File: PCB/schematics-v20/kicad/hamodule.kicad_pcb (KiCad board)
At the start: 2 copper layers, 78.4 x 84.3 mm, 104 parts, among them J1 GND|5V, J10 USB_C_Receptacle_USB2.0, J11 2604-1104, J12 2604-1104, J13 EspSense, J2 Conn_01x02_Male, J3 2604-1102, J4 USB | PS, J5 Conn_01x02_Male, J6 GND|3.3V, J7 Conn_01x02_Male, J8 Current Jumper, J9 EspRelays, K1 AQG12205, K2 AQG12205, K3 AQG12205, K4 AQG12205, Q1 SS8050-SMD, Q2 SS8050, SW1 Switch, SW2 Switch, U1 LD1117AV33, U2 ESP32-WROOM-32E, U3 CP2102N-A01-GQFN28, U4 ULN2003A, U5 LDA210-PDIP, U6 LDA210-PDIP, U7 SHT4x

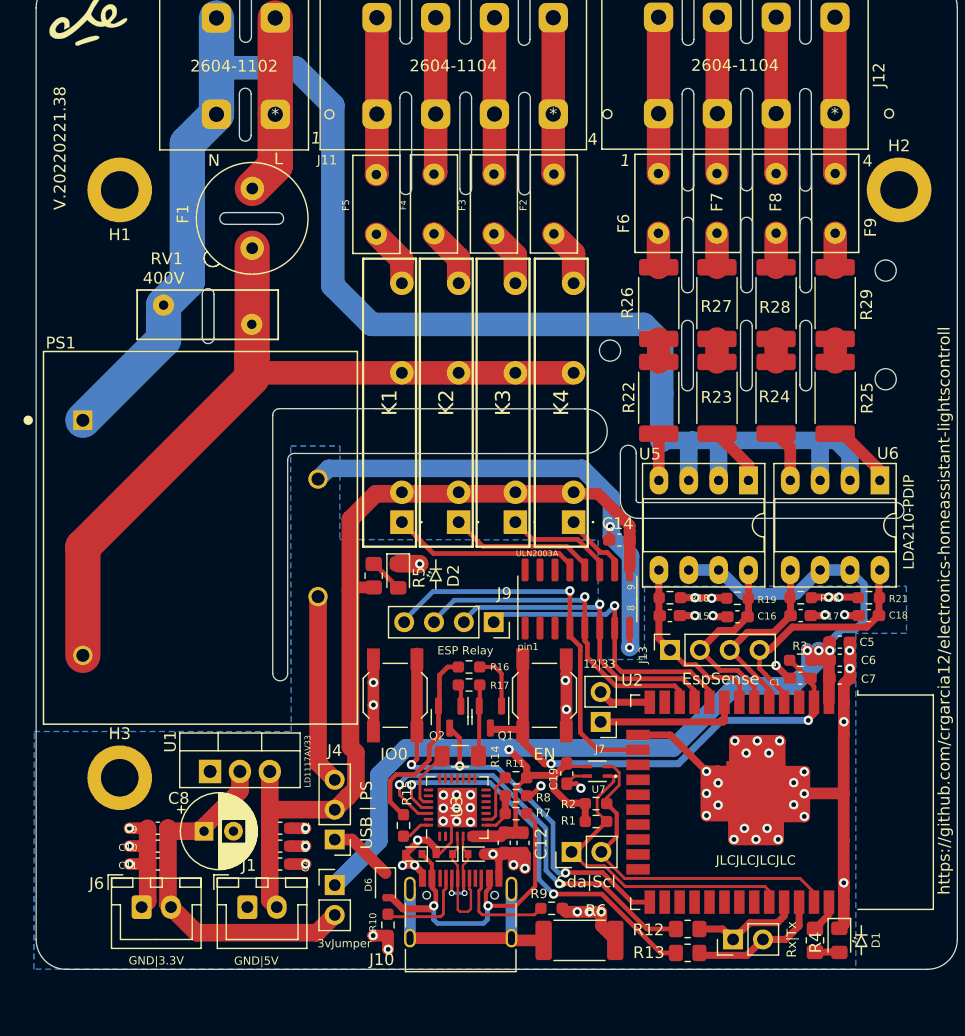
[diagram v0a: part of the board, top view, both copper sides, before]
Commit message: [V20] Move Earth;arrange minors;prod files
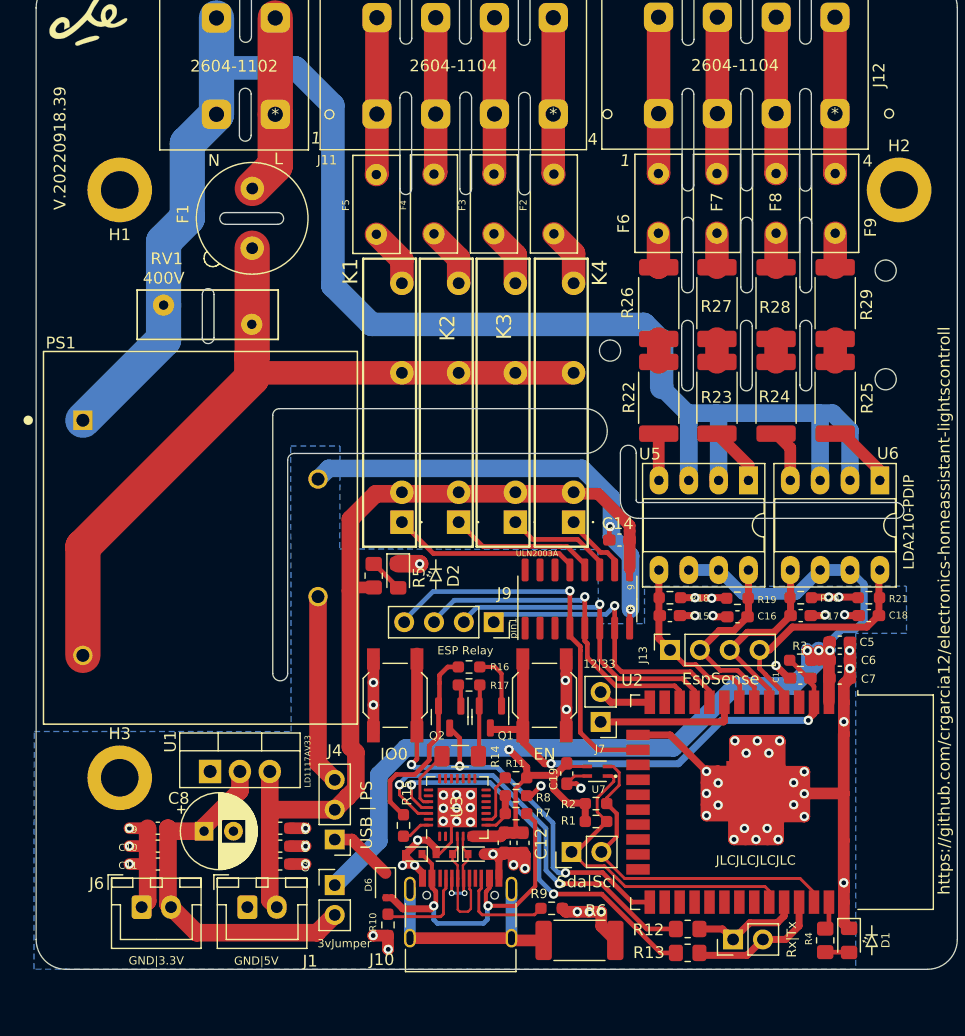
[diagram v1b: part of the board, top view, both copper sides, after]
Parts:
- moved G3 6.21 mm to (136.0, 115.2)
- moved NT1 4.51 mm to (178.4, 100.2)
- moved G2 0.89 mm to (196.1, 149.2)
- moved R4 0.87 mm to (192.3, 149.2)
- moved D1 0.83 mm to (194.3, 149.2)
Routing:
- net 220VAC(N)-LowV: track 29.2 -> 39.1 mm
- net 220VAC(N): track 99.8 -> 95.5 mm
- net GND: track 268.8 -> 265.5 mm
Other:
- outline, holes or cut-outs redrawn
- board text added: "V.20220918.39"
- board text removed: "V.20220221.38"

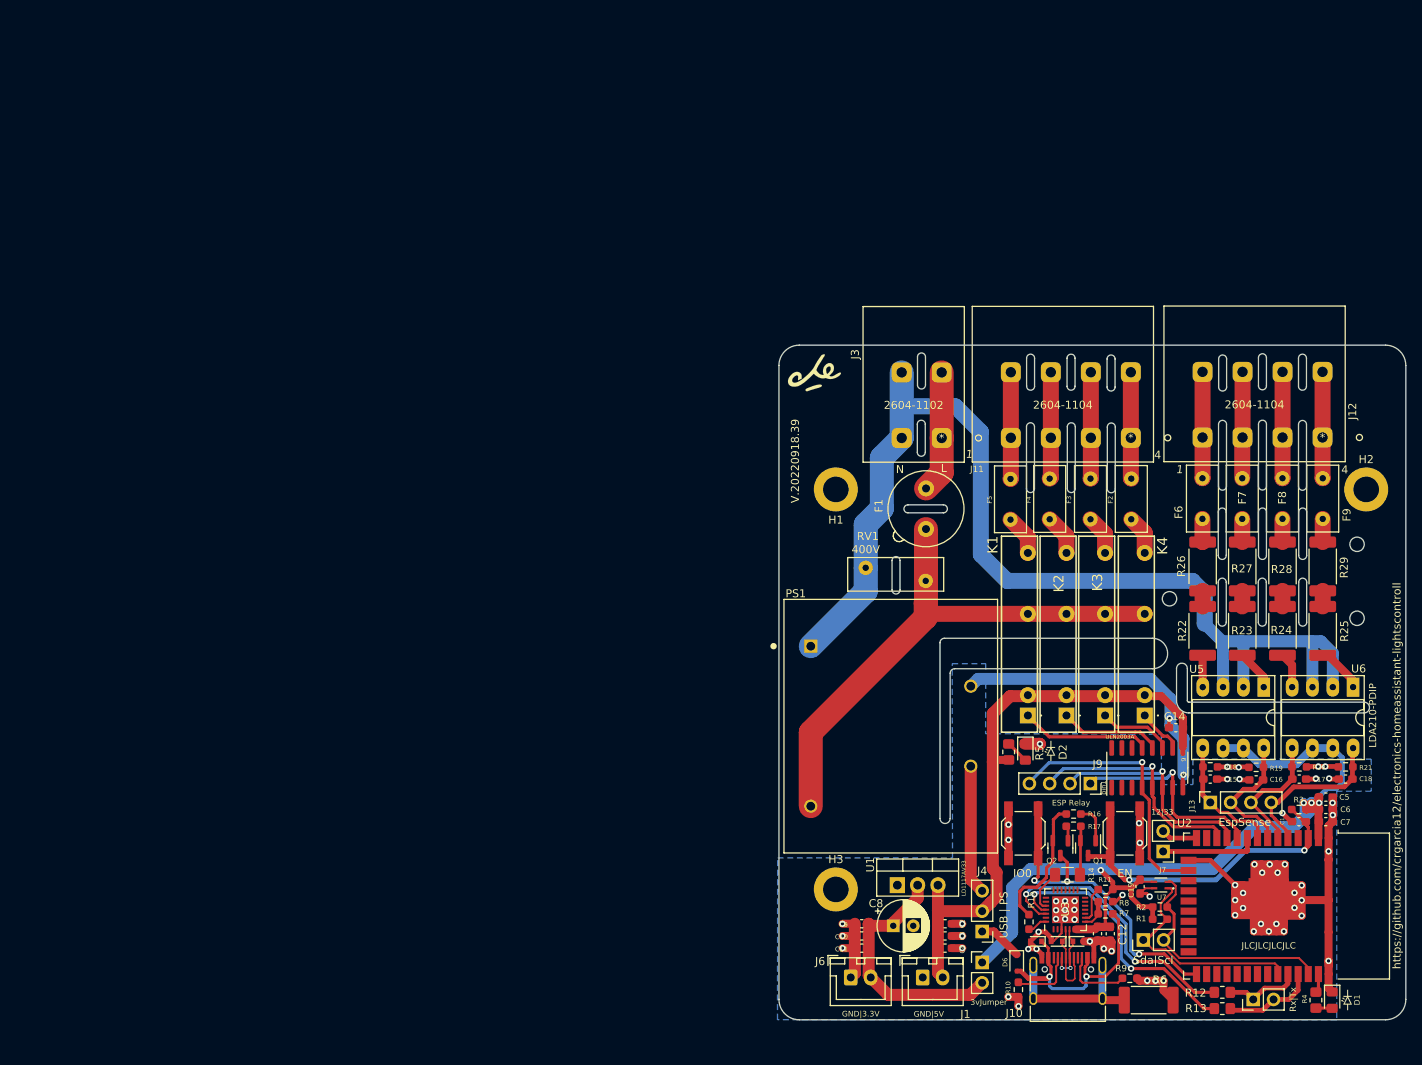
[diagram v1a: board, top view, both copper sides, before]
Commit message: [V20] updating Version;page settings;readme;pcb image
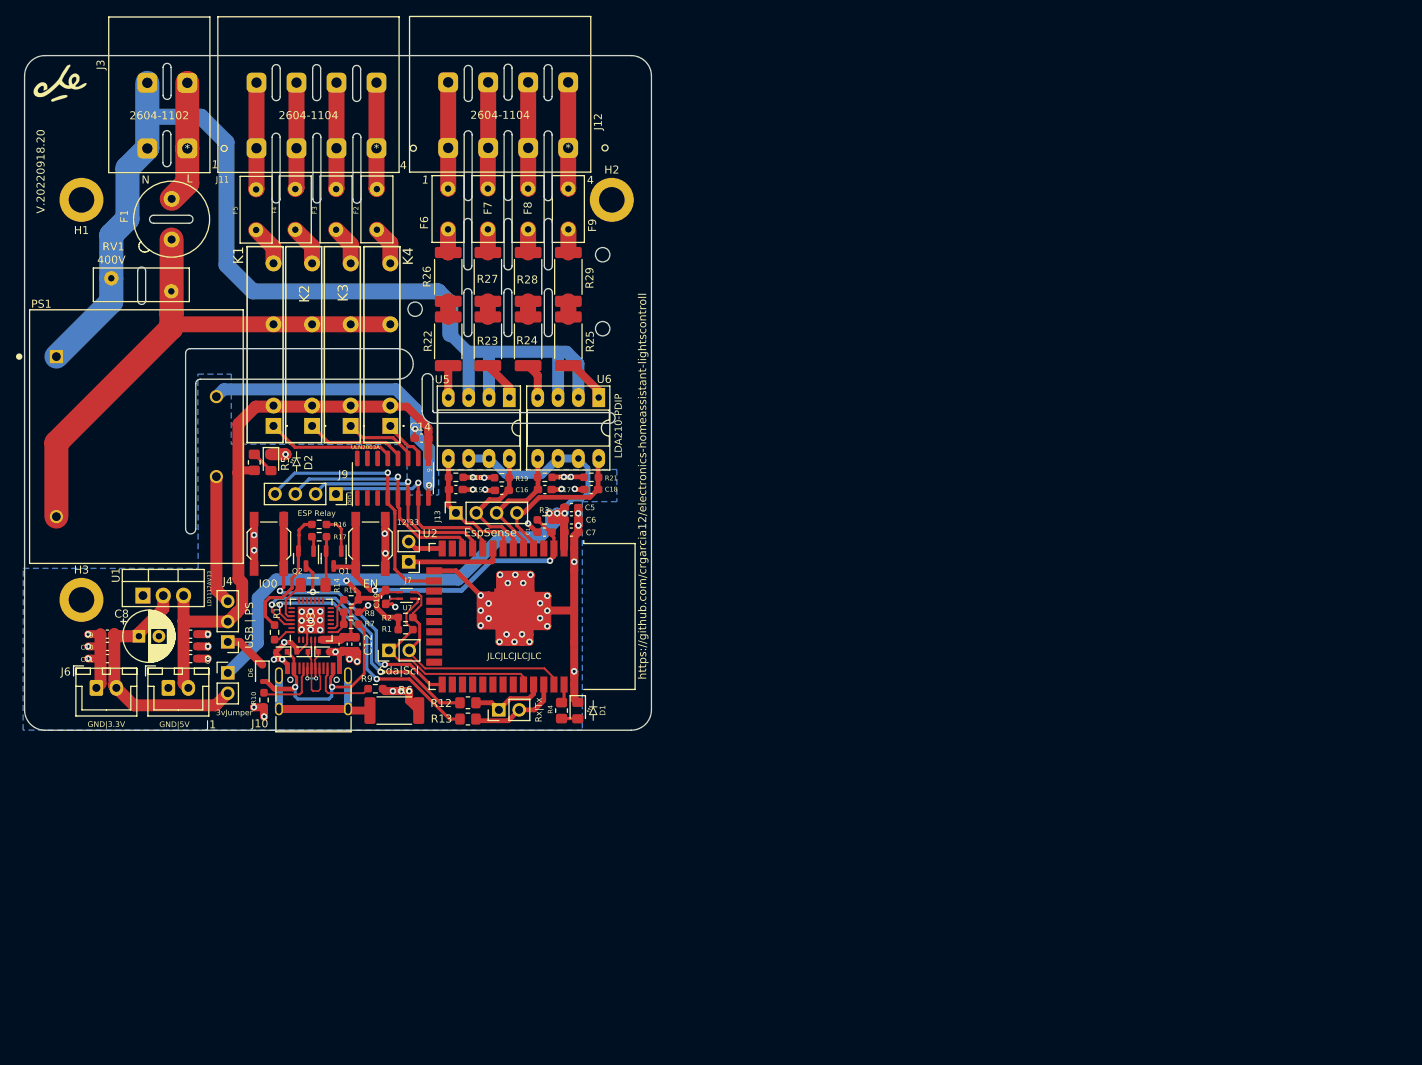
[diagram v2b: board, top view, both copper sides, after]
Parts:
- moved C1 101.0 mm to (95.9, 90.7)
- moved C12 101.0 mm to (72.3, 104.8)
- moved C14 101.0 mm to (80.5, 79.0)
- moved C15 101.0 mm to (84.8, 85.4)
- moved C19 101.0 mm to (76.0, 98.9)
- moved D5 101.0 mm to (65.6, 105.7)
- moved F1 101.0 mm to (49.2, 49.1)
- moved F7 101.0 mm to (88.8, 50.4)
- moved F8 101.0 mm to (93.8, 50.4)
- moved G*** 101.0 mm to (69.9, 89.6)
- moved H2 101.0 mm to (104.3, 49.2)
- moved J12 101.0 mm to (98.8, 42.7)
- moved J13 101.0 mm to (84.8, 88.3)
- moved J2 101.0 mm to (76.4, 105.5)
- moved J4 101.0 mm to (56.3, 104.5)
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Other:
- board text added: "V.20220918.20"
- board text removed: "V.20220918.39"

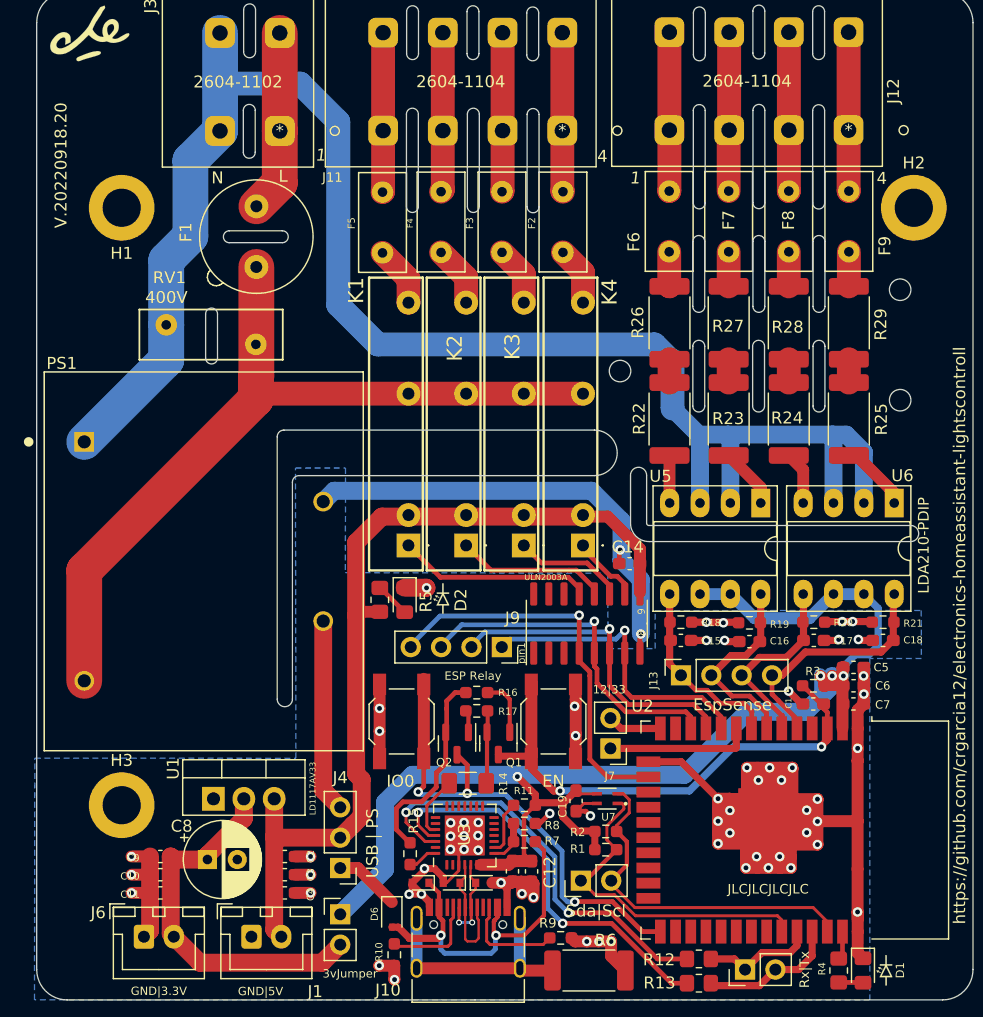
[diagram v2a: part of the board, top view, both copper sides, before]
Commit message: routed neutral; silkscreen; new images; prd files; remove testing files
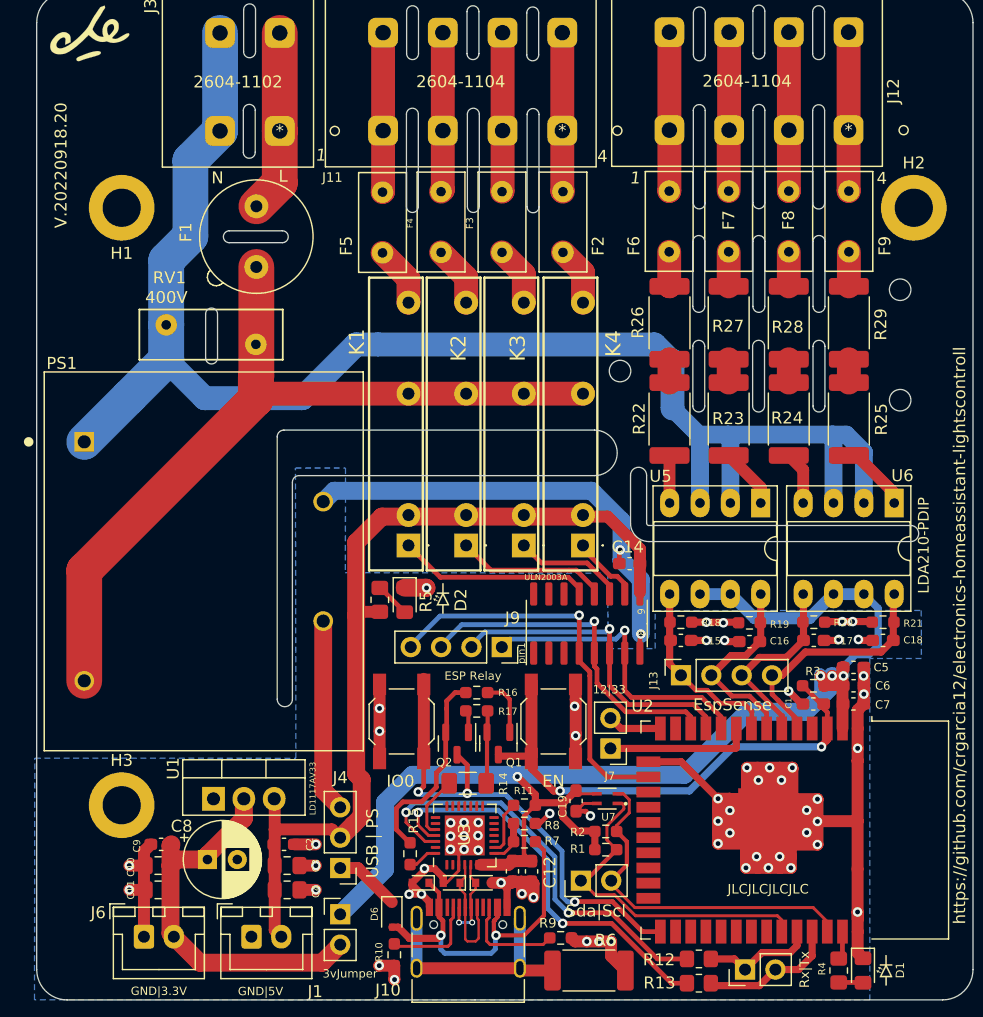
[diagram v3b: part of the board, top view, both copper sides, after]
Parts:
- C10, C11, C3, C4: footprint Capacitor_SMD:C_0603_1608Metric_Pad1.08x0.95mm_HandSolder -> Capacitor_SMD:C_0805_2012Metric_Pad1.18x1.45mm_HandSolder
- C5: value 22uF -> NC
- moved C2 1.02 mm to (51.6, 102.5)
- moved C9 1.02 mm to (41.3, 102.5)
- moved C10 0.79 mm to (41.0, 104.3)
- moved C3 0.79 mm to (51.8, 104.3)
- moved C11 0.32 mm to (41.0, 106.3)
- moved C4 0.32 mm to (51.8, 106.3)
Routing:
- net 220VAC(N): track 95.5 -> 85.3 mm
- net Net-(C10-Pad1): track 31.8 -> 33.0 mm
- net GND: track 265.5 -> 265.3 mm, vias 68 -> 67

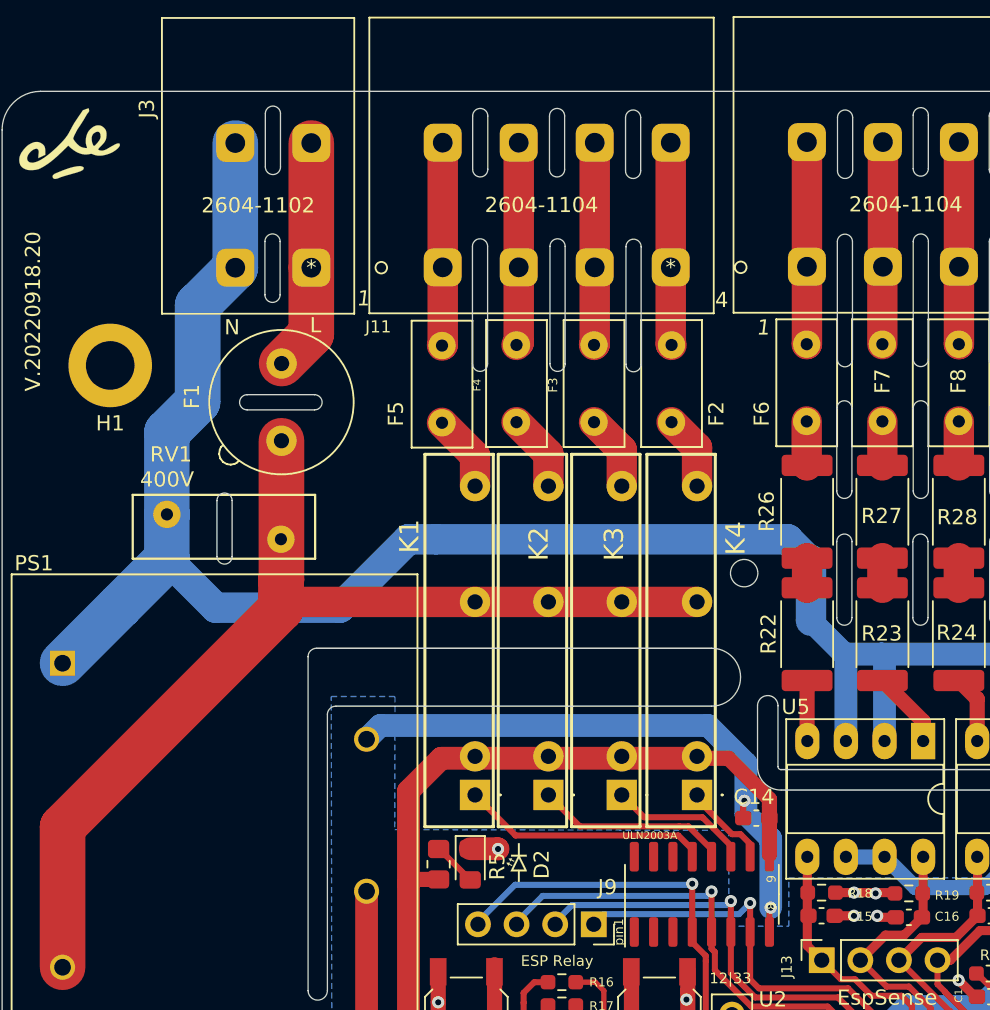
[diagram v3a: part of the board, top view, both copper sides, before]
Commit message: [V20] reorder fuses;mark icons as non schematic;prod files
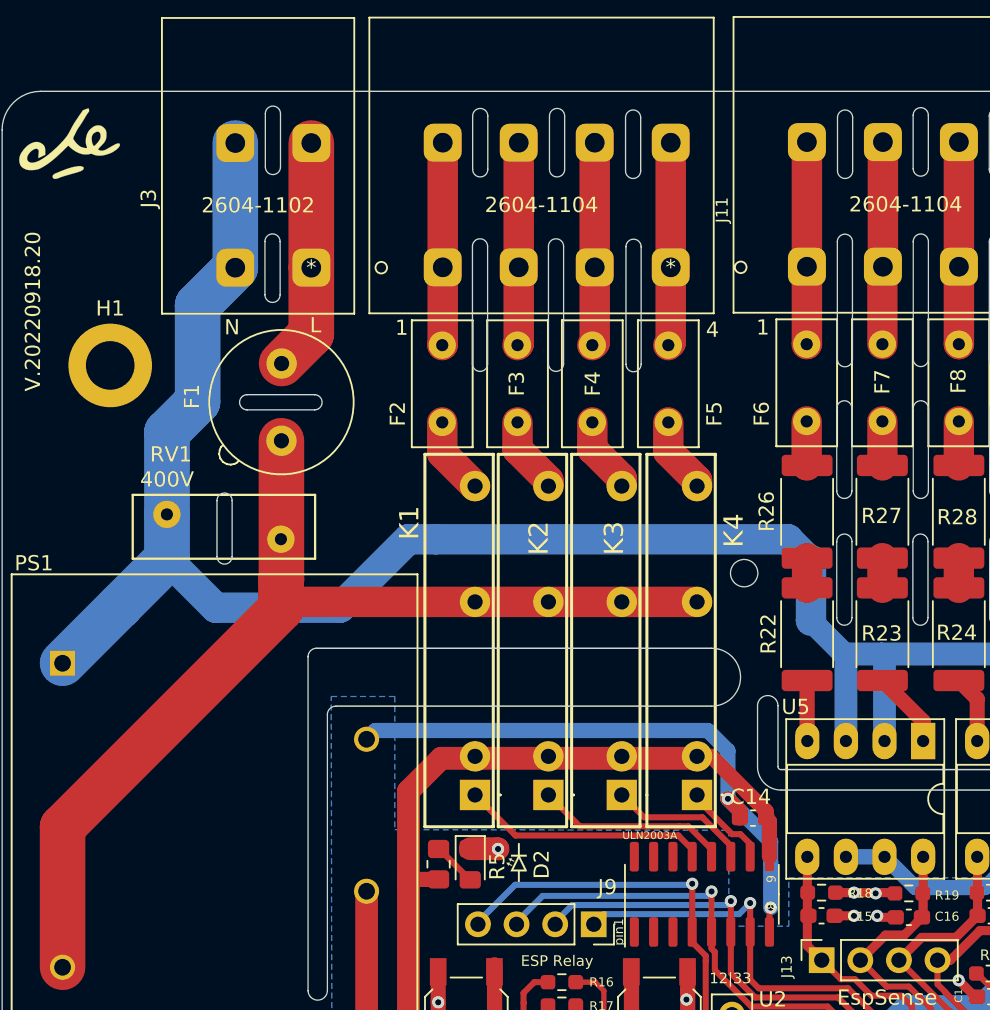
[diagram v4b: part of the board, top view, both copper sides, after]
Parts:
- Q1: value SS8050-SMD -> SS8050
- moved F2 15.1 mm to (59.8, 50.4)
- moved F5 14.9 mm to (74.7, 50.4)
- moved F3 5.03 mm to (64.8, 50.4)
- moved F4 4.99 mm to (69.7, 50.4)
- moved C14 0.22 mm to (80.3, 79.0)
- renumbered G2 to G4, G*** to G5, G*** to G6, G*** to G7
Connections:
- F2 pad 1: REO4 -> REO1
- F2 pad 2: Net-(F2-Pad2) -> Net-(J11-Pad7)
- F3 pad 1: REO3 -> REO2
- F3 pad 2: Net-(F3-Pad2) -> Net-(J11-Pad5)
- F4 pad 1: REO2 -> REO3
- F4 pad 2: Net-(F4-Pad2) -> Net-(J11-Pad3)
- F5 pad 1: REO1 -> REO4
- F5 pad 2: Net-(F5-Pad2) -> Net-(J11-Pad1)
- J11 pad 1: Net-(F2-Pad2) -> Net-(J11-Pad1)
- J11 pad 2: Net-(F2-Pad2) -> Net-(J11-Pad1)
- J11 pad 3: Net-(F3-Pad2) -> Net-(J11-Pad3)
- J11 pad 4: Net-(F3-Pad2) -> Net-(J11-Pad3)
- J11 pad 5: Net-(F4-Pad2) -> Net-(J11-Pad5)
- J11 pad 6: Net-(F4-Pad2) -> Net-(J11-Pad5)
- J11 pad 7: Net-(F5-Pad2) -> Net-(J11-Pad7)
- J11 pad 8: Net-(F5-Pad2) -> Net-(J11-Pad7)
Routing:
- net Net-(J11-Pad3): track 0.00 -> 13.4 mm
- net Net-(J11-Pad1): track 0.00 -> 13.4 mm
- net Net-(F4-Pad2): track 13.4 -> 0.00 mm
- net Net-(F5-Pad2): track 13.4 -> 0.00 mm
- net Net-(J11-Pad5): track 0.00 -> 13.4 mm
- net Net-(J11-Pad7): track 0.00 -> 13.3 mm
- net Net-(F2-Pad2): track 13.3 -> 0.00 mm
- net Net-(F3-Pad2): track 13.3 -> 0.00 mm
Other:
- outline, holes or cut-outs redrawn
